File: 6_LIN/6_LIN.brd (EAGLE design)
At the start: 67.4 x 44.8 mm, 11 parts, among them IC6 MCP2003, X12 ALLSERIALD, X6 AKL18X-03W

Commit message: change diodes
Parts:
- removed D3: (no value), microbuilder:SOD-123
- added C1: 220p, rcl:C0805
- added D5: 43V, diode:SOD80C
- added R2: 47, rcl:R0805
- C14: value 100n -> 1µ
- D1: value (none) -> 1N4148; device microbuilder:SOD-123 -> diode:MINIMELF
- D2: value (none) -> MMBZ27VAL; device microbuilder:SOD-123 -> diode:SOT23
- D4: value (none) -> 1N4148; device diode:SOT23 -> diode:MINIMELF
- moved D1 27.5 mm to (19.1, 29.2), turned to 90 degrees
- moved D4 18.3 mm to (1.27, 41.9)
- moved D2 18.2 mm to (12.7, 27.9), turned to 180 degrees
- moved R6 13.7 mm to (-5.08, 41.9), turned to 0 degrees
- moved J1 6.38 mm to (-12.7, 36.2)
- moved C14 4.02 mm to (5.08, 19.1), turned to 270 degrees
- moved IC6 4.02 mm to (8.89, 19.1)
- moved X6 2.62 mm to (12.7, 37.5)
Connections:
- removed net +12V: D1.A, X12.20
- removed net N$75: D3.C, R6.2
- removed net N$78: IC6.2, X12.1
- new net +UB: D1.A, D4.A, X6.P$1
- new net N$3: C14.1, D5.C, IC6.7, R2.1
- net +5V: now also IC6.2
- net GND: now also C1.2, D2.1, D5.A; no longer D4.1
- net N$1: now also R2.2; no longer D2.A, X6.P$1
- net N$2: now also D4.C, R6.2; no longer C14.1, D2.C, D3.A, IC6.7
- net N$73: now also C1.1, D2.2; no longer D4.3
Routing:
- net N$73: track 0.00 -> 46.5 mm
- net +5V: track 0.00 -> 28.7 mm, vias 0 -> 2
- net +UB: track 0.00 -> 26.6 mm
- net N$3: track 0.00 -> 23.7 mm, vias 0 -> 2
- net GND: track 0.00 -> 15.5 mm, vias 0 -> 5
- net N$79: track 0.00 -> 13.5 mm
- net N$74: track 0.00 -> 12.2 mm
- net N$77: track 0.00 -> 11.9 mm, vias 0 -> 2
- net N$2: track 0.00 -> 3.70 mm
- net N$1: track 0.00 -> 2.43 mm
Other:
- board text added: "AllSerial - LIN v1.0 30/18"

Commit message: add author
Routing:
- net GND: vias 5 -> 44
- added copper zone on layer 1, net GND
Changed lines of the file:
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@@
 <setting verticaltext="up"/>
 </settings>
-<grid distance="0.05" unitdist="inch" unit="mm" style="lines" multiple="1" display="no" altdistance="0.025" altunitdist="inch" altunit="inch"/>
+<grid distance="0.25" unitdist="inch" unit="inch" style="lines" multiple="1" display="yes" altdistance="0.0125" altunitdist="inch" altunit="inch"/>
 <layers>
 <layer number="1" name="Top" color="4" fill="1" visible="yes" active="yes"/>
@@
 </class>
 </classes>
-<designrules name="default *">
+<designrules name="Elecrow_2-layer_PCB_eagle_rule *">
 <description language="de">&lt;b&gt;EAGLE Design Rules&lt;/b&gt;
 &lt;p&gt;
@@
 necessary adjustments and save your customized
 design rules under a new name.</description>
+<description language="zh">&lt;b&gt;Elecrow PCB EAGLE Design Rules&lt;/b&gt;
+</description>
 <param name="layerSetup" value="(1*16)"/>
 <param name="mtCopper" value="0.035mm 0.035mm 0.035mm 0.035mm 0.035mm 0.035mm 0.035mm 0.035mm 0.035mm 0.035mm 0.035mm 0.035mm 0.035mm 0.035mm 0.035mm 0.035mm"/>
-<param name="mtIsolate" value="1.5mm 0.15mm 0.2mm 0.15mm 0.2mm 0.15mm 0.2mm 0.15mm 0.2mm 0.15mm 0.2mm 0.15mm 0.2mm 0.15mm 0.2mm"/>
-<param name="mdWireWire" value="8mil"/>
-<param name="mdWirePad" value="8mil"/>
-<param name="mdWireVia" value="8mil"/>
-<param name="mdPadPad" value="8mil"/>
-<param name="mdPadVia" value="8mil"/>
+<param name="mtIsolate" value="1.6mm 1.2mm 0.2mm 0.15mm 0.2mm 0.15mm 0.2mm 0.15mm 0.2mm 0.15mm 0.2mm 0.15mm 0.2mm 0.15mm 0.2mm"/>
+<param name="mdWireWire" value="6mil"/>
+<param name="mdWirePad" value="6mil"/>
+<param name="mdWireVia" value="6mil"/>
+<param name="mdPadPad" value="6mil"/>
+<param name="mdPadVia" value="6mil"/>
 <param name="mdViaVia" value="8mil"/>
-<param name="mdSmdPad" value="8mil"/>
-<param name="mdSmdVia" value="8mil"/>
-<param name="mdSmdSmd" value="8mil"/>
+<param name="mdSmdPad" value="0mil"/>
+<param name="mdSmdVia" value="0mil"/>
+<param name="mdSmdSmd" value="0mil"/>
 <param name="mdViaViaSameLayer" value="8mil"/>
 <param name="mnLayersViaInSmd" value="2"/>
-<param name="mdCopperDimension" value="40mil"/>
-<param name="mdDrill" value="8mil"/>
+<param name="mdCopperDimension" value="20mil"/>
+<param name="mdDrill" value="10mil"/>
 <param name="mdSmdStop" value="0mil"/>
-<param name="msWidth" value="10mil"/>
-<param name="msDrill" value="24mil"/>
-<param name="msMicroVia" value="9.99mm"/>
+<param name="msWidth" value="6mil"/>
+<param name="msDrill" value="0.3mm"/>
+<param name="msMicroVia" value="12mil"/>
 <param name="msBlindViaRatio" value="0.5"/>
 <param name="rvPadTop" value="0.25"/>
@@
 <param name="rvMicroViaOuter" value="0.25"/>
 <param name="rvMicroViaInner" value="0.25"/>
-<param name="rlMinPadTop" value="10mil"/>
+<param name="rlMinPadTop" value="6mil"/>
 <param name="rlMaxPadTop" value="20mil"/>
-<param name="rlMinPadInner" value="10mil"/>
+<param name="rlMinPadInner" value="6mil"/>
 <param name="rlMaxPadInner" value="20mil"/>
-<param name="rlMinPadBottom" value="10mil"/>
+<param name="rlMinPadBottom" value="6mil"/>
 <param name="rlMaxPadBottom" value="20mil"/>
-<param name="rlMinViaOuter" value="8mil"/>
+<param name="rlMinViaOuter" value="6mil"/>
 <param name="rlMaxViaOuter" value="20mil"/>
-<param name="rlMinViaInner" value="8mil"/>
+<param name="rlMinViaInner" value="6mil"/>
 <param name="rlMaxViaInner" value="20mil"/>
 <param name="rlMinMicroViaOuter" value="4mil"/>
@@
 <param name="psTop" value="-1"/>
 <param name="psBottom" value="-1"/>
-<param name="psFirst" value="-1"/>
+<param name="psFirst" value="0"/>
 <param name="psElongationLong" value="100"/>
 <param name="psElongationOffset" value="100"/>
 <param name="mvStopFrame" value="1"/>
 <param name="mvCreamFrame" value="0"/>
-<param name="mlMinStopFrame" value="4mil"/>
-<param name="mlMaxStopFrame" value="4mil"/>
+<param name="mlMinStopFrame" value="0mil"/>
+<param name="mlMaxStopFrame" value="0mil"/>
 <param name="mlMinCreamFrame" value="0mil"/>
 <param name="mlMaxCreamFrame" value="0mil"/>
@@
 <param name="checkAngle" value="0"/>
 <param name="checkFont" value="1"/>
-<param name="checkRestrict" value="1"/>
+<param name="checkRestrict" value="0"/>
 <param name="useDiameter" value="13"/>
 <param name="maxErrors" value="50"/>
@@
 <element name="X6" library="con-riacon_akl" package="AKL182-03" value="AKL18X-03W" x="12.7" y="37.465" smashed="yes" rot="R180">
 <attribute name="VALUE" x="19.685" y="41.91" size="1.016" layer="27"/>
-<attribute name="NAME" x="19.05" y="38.735" size="1.016" layer="25" rot="R270"/>
+<attribute name="NAME" x="19.05" y="37.465" size="1.016" layer="25" rot="R270"/>
 </element>
 <element name="C14" library="rcl" package="C0805" value="1µ" x="5.08" y="19.05" smashed="yes" rot="R270">
@@
 </element>
 <element name="C1" library="rcl" package="C0805" value="220p" x="10.795" y="33.02" smashed="yes" rot="R180">
-<attribute name="NAME" x="7.62" y="33.02" size="1.016" layer="25" rot="R180"/>
+<attribute name="NAME" x="7.62" y="33.3375" size="1.016" layer="25" rot="R180"/>
 <attribute name="VALUE" x="5.08" y="33.655" size="1.016" layer="27"/>
 </element>
@@
 <wire x1="5.08" y1="18.1" x2="5.08" y2="16.51" width="0.4064" layer="1"/>
 <via x="5.08" y="16.51" extent="1-16" drill="0.3"/>
+<polygon width="0.254" layer="1" isolate="0.3048">
+<vertex x="-34.29" y="0"/>
+<vertex x="34.29" y="0"/>
+<vertex x="34.29" y="45.72"/>
+<vertex x="-34.29" y="45.72"/>
+</polygon>
+<via x="-25.4" y="38.1" extent="1-16" drill="0.3"/>
+<via x="-25.4" y="31.75" extent="1-16" drill="0.3"/>
+<via x="-25.4" y="25.4" extent="1-16" drill="0.3"/>
+<via x="-25.4" y="19.05" extent="1-16" drill="0.3"/>
+<via x="-25.4" y="12.7" extent="1-16" drill="0.3"/>
+<via x="-25.4" y="6.35" extent="1-16" drill="0.3"/>
+<via x="25.4" y="38.1" extent="1-16" drill="0.3"/>
+<via x="25.4" y="31.75" extent="1-16" drill="0.3"/>
+<via x="25.4" y="25.4" extent="1-16" drill="0.3"/>
+<via x="25.4" y="19.05" extent="1-16" drill="0.3"/>
+<via x="25.4" y="12.7" extent="1-16" drill="0.3"/>
+<via x="25.4" y="6.35" extent="1-16" drill="0.3"/>
+<via x="-19.05" y="31.75" extent="1-16" drill="0.3"/>
+<via x="-19.05" y="25.4" extent="1-16" drill="0.3"/>
+<via x="-19.05" y="19.05" extent="1-16" drill="0.3"/>
+<via x="-19.05" y="12.7" extent="1-16" drill="0.3"/>
+<via x="-12.7" y="31.75" extent="1-16" drill="0.3"/>
+<via x="-12.7" y="25.4" extent="1-16" drill="0.3"/>
+<via x="-12.7" y="19.05" extent="1-16" drill="0.3"/>
+<via x="-12.7" y="12.7" extent="1-16" drill="0.3"/>
+<via x="-6.35" y="31.75" extent="1-16" drill="0.3"/>
+<via x="-6.35" y="25.4" extent="1-16" drill="0.3"/>
+<via x="-6.35" y="19.05" extent="1-16" drill="0.3"/>
+<via x="-6.35" y="12.7" extent="1-16" drill="0.3"/>
+<via x="0" y="31.75" extent="1-16" drill="0.3"/>
+<via x="0" y="25.4" extent="1-16" drill="0.3"/>
+<via x="0" y="19.05" extent="1-16" drill="0.3"/>
+<via x="0" y="12.7" extent="1-16" drill="0.3"/>
+<via x="-19.05" y="6.35" extent="1-16" drill="0.3"/>
+<via x="-19.05" y="38.1" extent="1-16" drill="0.3"/>
+<via x="19.05" y="38.1" extent="1-16" drill="0.3"/>
+<via x="19.05" y="6.35" extent="1-16" drill="0.3"/>
+<via x="12.7" y="12.7" extent="1-16" drill="0.3"/>
+<via x="6.35" y="31.75" extent="1-16" drill="0.3"/>
+<via x="6.35" y="25.4" extent="1-16" drill="0.3"/>
+<via x="-6.35" y="38.1" extent="1-16" drill="0.3"/>
+<via x="0" y="38.1" extent="1-16" drill="0.3"/>
+<via x="6.35" y="38.1" extent="1-16" drill="0.3"/>
+<via x="19.05" y="12.7" extent="1-16" drill="0.3"/>
 </signal>
 <signal name="N$73">

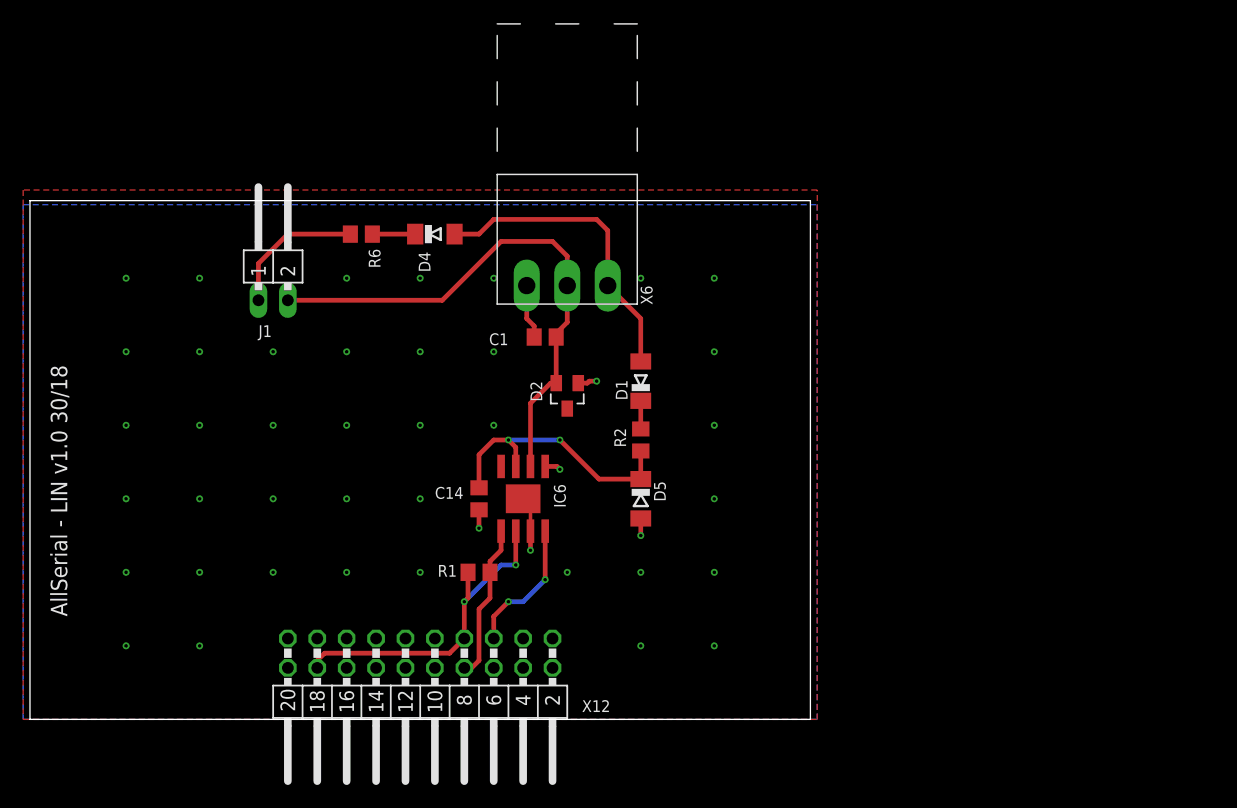
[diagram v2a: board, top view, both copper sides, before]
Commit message: new lib, change pinout!
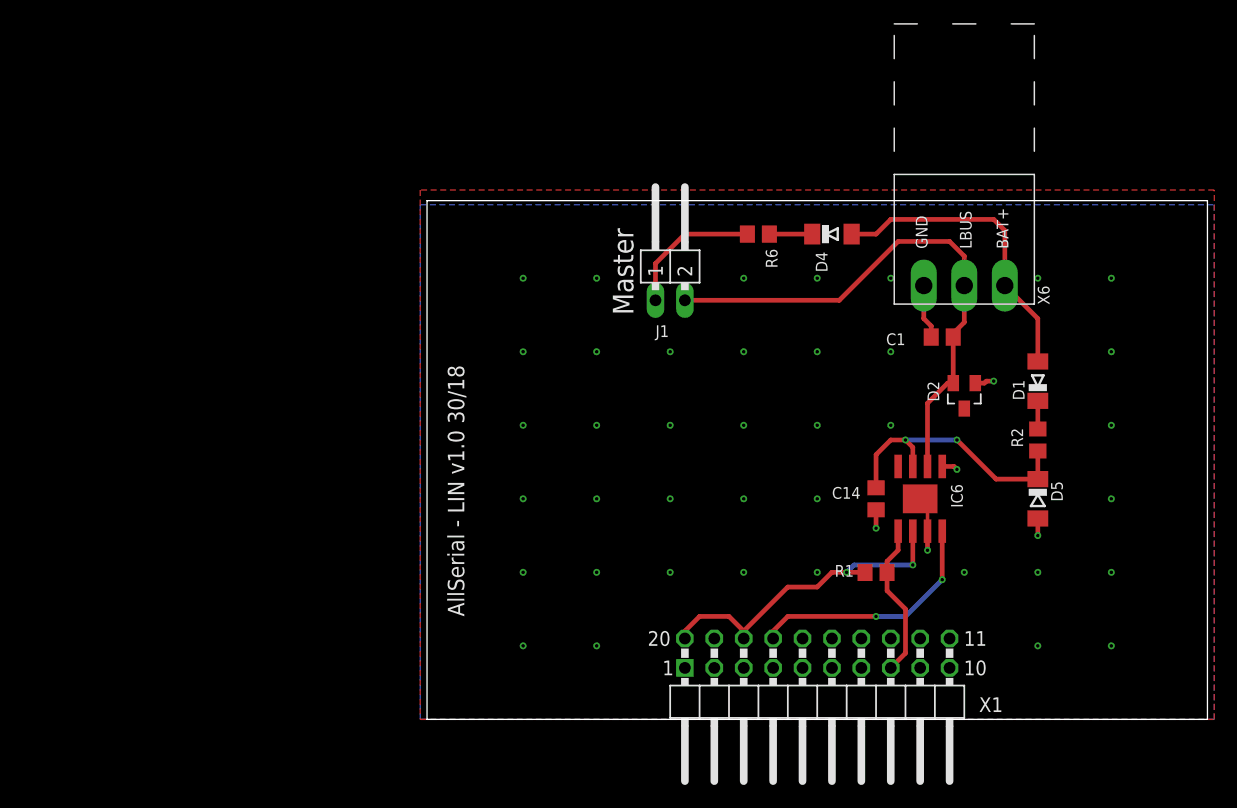
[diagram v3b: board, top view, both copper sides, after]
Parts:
- removed X12: ALLSERIALD, AllSerial:DAUGHTER-THT
- added X1: ALLSERIALSLAVE, AllSerialv2:DAUGHTER-THT
- moved D1 34.3 mm to (53.3, 29.2)
- moved D2 34.3 mm to (47.0, 27.9)
- moved D5 34.3 mm to (53.3, 19.1)
- moved R2 34.3 mm to (53.3, 24.1)
- moved X6 34.3 mm to (47.0, 37.5)
- moved C1 34.3 mm to (45.1, 33.0)
- moved C14 34.3 mm to (39.4, 19.1)
- moved D4 34.3 mm to (35.6, 41.9)
- moved IC6 34.3 mm to (43.2, 19.1)
- moved J1 34.3 mm to (21.6, 36.2)
- moved R1 34.3 mm to (39.4, 12.7)
- moved R6 34.3 mm to (29.2, 41.9)
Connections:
- net +5V: now also X1.18, X1.20; no longer X12.18, X12.7
- net GND: now also X1.1; no longer X12.19
- net N$77: now also X1.17; no longer X12.5
- net N$79: now also X1.8; no longer X12.8
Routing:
- net N$77: track 11.9 -> 21.3 mm
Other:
- board text added: "BAT+"
- board text added: "GND"
- board text added: "LBUS"
- board text added: "Master"
